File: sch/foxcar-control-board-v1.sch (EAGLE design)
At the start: 91 parts, among them Q1 PSMN1R2-30YLC, U1 HMC5883LSMD, U2 SPX29300

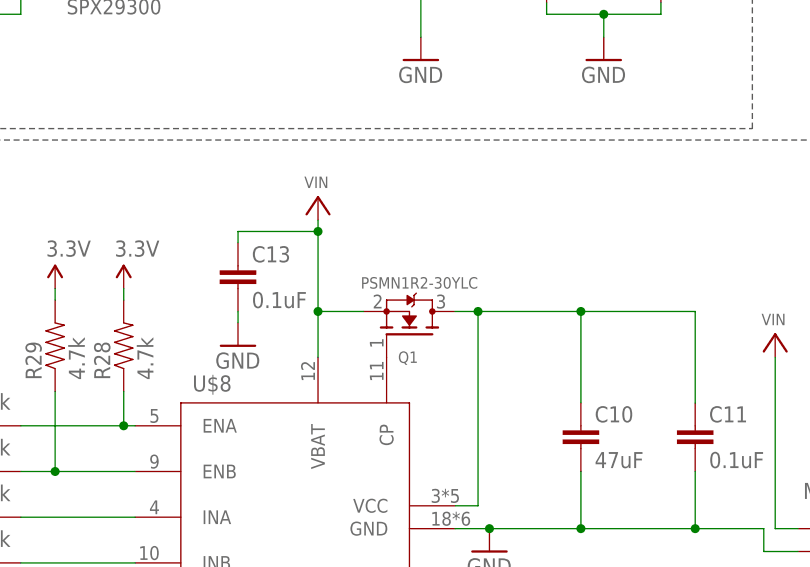
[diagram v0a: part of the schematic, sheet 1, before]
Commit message: Set up Eagle board with Sparkfun 4-layer DRU. Set up layers. Started with power section.
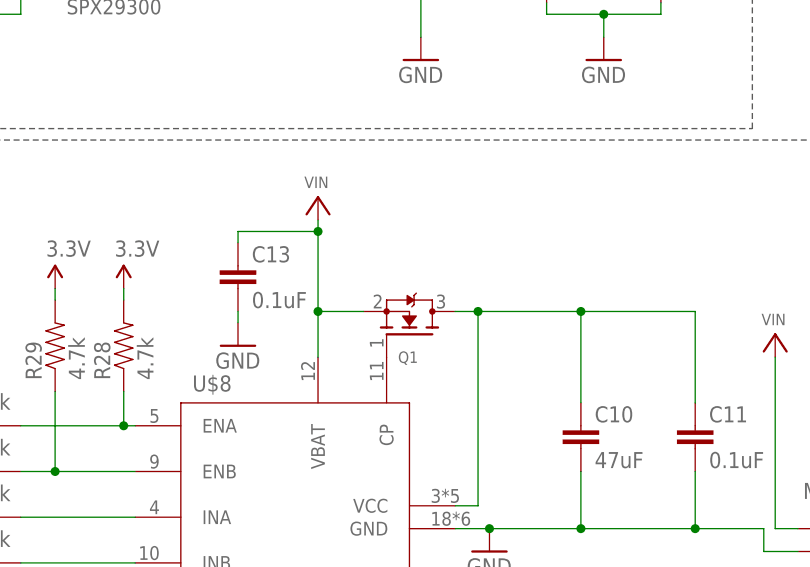
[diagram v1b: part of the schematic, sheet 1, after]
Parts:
- Q1: value PSMN1R2-30YLC -> (none)
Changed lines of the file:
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@@
 <part name="DIG_GND16" library="SparkFun-Aesthetics" deviceset="GND" device="" value="GND"/>
 <part name="DIG_GND17" library="SparkFun-Aesthetics" deviceset="GND" device="" value="GND"/>
-<part name="Q1" library="adafruit" deviceset="MOSFET-N" device="REFLOW" value="PSMN1R2-30YLC"/>
+<part name="Q1" library="adafruit" deviceset="MOSFET-N" device="REFLOW"/>
 <part name="GND12" library="SparkFun-Aesthetics" deviceset="GND" device=""/>
 <part name="JP20" library="SparkFun-Connectors" deviceset="M04" device="SCREW_LOCK" value="MOTORS"/>

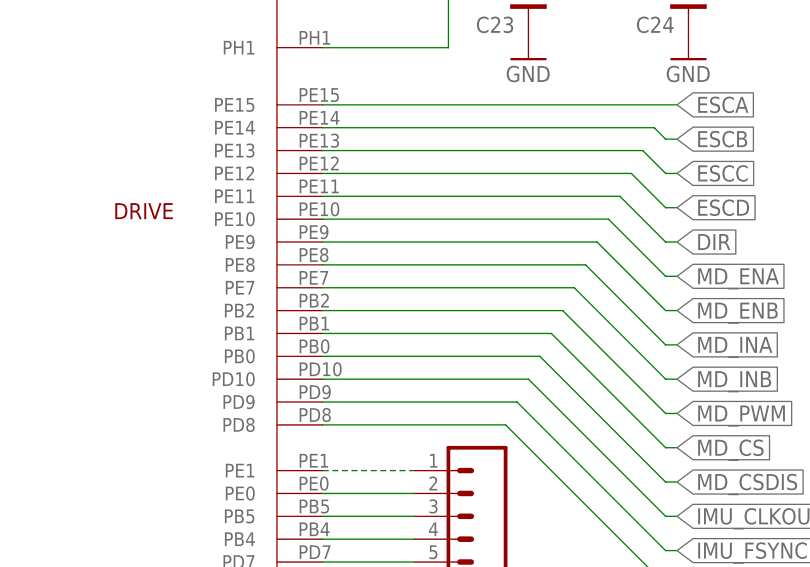
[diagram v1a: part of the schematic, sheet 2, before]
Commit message: Almost done with power layout. Minor stm32 symbol changes.
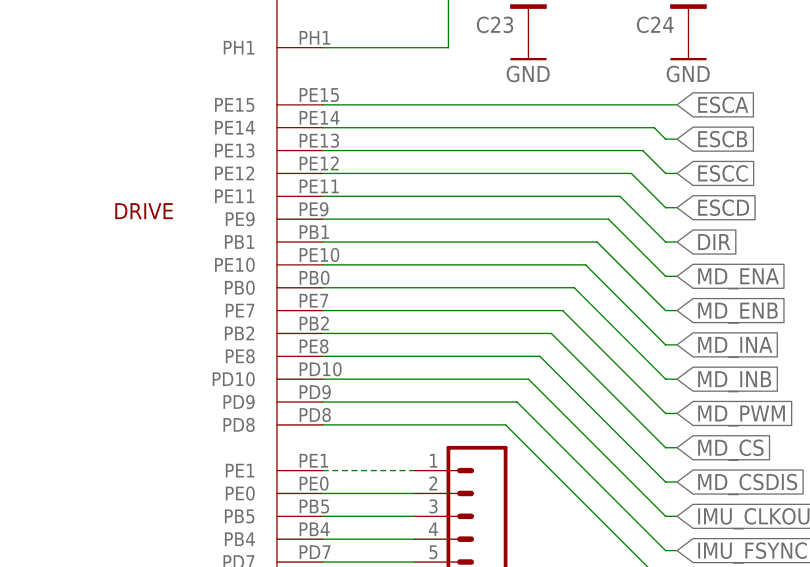
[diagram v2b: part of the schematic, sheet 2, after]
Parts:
- renumbered LED4 to LED2
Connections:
- net N$76 renamed INB
- net N$77 renamed CP
- net N$78 renamed VCC
- net N$79 renamed INA
- net N$83 renamed ENB
- net N$84 renamed ENA
- net N$85 renamed PWM
- net N$86 renamed CS
- removed net N$80: JP20.3, U$8.OUTA
- removed net N$81: JP20.4, U$8.OUTB
- new net OUTA: JP20.4, U$8.OUTA
- new net OUTB: JP20.3, U$8.OUTB
- net MD_CS: now also U$10.PB2; no longer U$10.PB1
- net MD_CSDIS: now also U$10.PE8; no longer U$10.PB0
- net MD_ENA: now also U$10.PE9; no longer U$10.PE10
- net MD_ENB: now also U$10.PB1; no longer U$10.PE9
- net MD_INA: now also U$10.PE10; no longer U$10.PE8
- net MD_INB: now also U$10.PB0; no longer U$10.PE7
- net MD_PWM: now also U$10.PE7; no longer U$10.PB2
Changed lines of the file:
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@@
 <part name="U$12" library="SparkFun-Aesthetics" deviceset="VIN" device=""/>
 <part name="LED3" library="led" deviceset="LED" device="CHIP-LED0603" value="GREEN"/>
-<part name="LED4" library="led" deviceset="LED" device="CHIP-LED0603" value="GREEN"/>
+<part name="LED2" library="led" deviceset="LED" device="CHIP-LED0603" value="GREEN"/>
 <part name="R1" library="SparkFun-Passives" deviceset="RESISTOR" device="0402-RES" value="270"/>
 <part name="R3" library="SparkFun-Passives" deviceset="RESISTOR" device="0402-RES" value="50"/>
@@
 <instance part="U$12" gate="G$1" x="-110.49" y="95.25"/>
 <instance part="LED3" gate="G$1" x="-40.64" y="91.44"/>
-<instance part="LED4" gate="G$1" x="-27.94" y="91.44"/>
+<instance part="LED2" gate="G$1" x="-27.94" y="91.44"/>
 <instance part="R1" gate="G$1" x="-40.64" y="80.01" rot="R90"/>
 <instance part="R3" gate="G$1" x="-27.94" y="80.01" rot="R90"/>
@@
 </segment>
 <segment>
-<pinref part="LED4" gate="G$1" pin="A"/>
+<pinref part="LED2" gate="G$1" pin="A"/>
 <wire x1="-27.94" y1="95.25" x2="-27.94" y2="93.98" width="0.15" layer="91"/>
 <pinref part="P+30" gate="G$1" pin="3.3V"/>
@@
 </segment>
 </net>
-<net name="N$77" class="0">
+<net name="CP" class="0">
 <segment>
 <pinref part="Q1" gate="G$1" pin="G"/>
@@
 </segment>
 </net>
-<net name="N$78" class="0">
+<net name="VCC" class="0">
 <segment>
 <pinref part="U$8" gate="G$1" pin="VCC"/>
@@
 </segment>
 </net>
-<net name="N$80" class="0">
-<segment>
-<pinref part="U$8" gate="G$1" pin="OUTA"/>
-<wire x1="-50.8" y1="8.89" x2="-16.51" y2="8.89" width="0.15" layer="91"/>
+<net name="OUTB" class="0">
+<segment>
 <wire x1="-16.51" y1="8.89" x2="-16.51" y2="11.43" width="0.15" layer="91"/>
 <pinref part="JP20" gate="G$1" pin="3"/>
 <wire x1="-16.51" y1="11.43" x2="-12.7" y2="11.43" width="0.15" layer="91"/>
-</segment>
-</net>
-<net name="N$81" class="0">
+<pinref part="U$8" gate="G$1" pin="OUTB"/>
+<wire x1="-50.8" y1="8.89" x2="-16.51" y2="8.89" width="0.15" layer="91"/>
+</segment>
+</net>
+<net name="OUTA" class="0">
 <segment>
 <pinref part="JP20" gate="G$1" pin="4"/>
 <wire x1="-12.7" y1="8.89" x2="-15.24" y2="8.89" width="0.15" layer="91"/>
 <wire x1="-15.24" y1="8.89" x2="-15.24" y2="6.35" width="0.15" layer="91"/>
-<pinref part="U$8" gate="G$1" pin="OUTB"/>
+<pinref part="U$8" gate="G$1" pin="OUTA"/>
 <wire x1="-15.24" y1="6.35" x2="-50.8" y2="6.35" width="0.15" layer="91"/>
 </segment>
 </net>
-<net name="N$86" class="0">
+<net name="CS" class="0">
 <segment>
 <pinref part="U$8" gate="G$1" pin="CS"/>
@@
 </segment>
 </net>
-<net name="N$85" class="0">
+<net name="PWM" class="0">
 <segment>
 <pinref part="U$8" gate="G$1" pin="PWM"/>
@@
 </segment>
 </net>
-<net name="N$76" class="0">
+<net name="INB" class="0">
 <segment>
 <pinref part="U$8" gate="G$1" pin="INB"/>
@@
 </segment>
 </net>
-<net name="N$79" class="0">
+<net name="INA" class="0">
 <segment>
 <pinref part="U$8" gate="G$1" pin="INA"/>
@@
 </segment>
 </net>
-<net name="N$83" class="0">
+<net name="ENB" class="0">
 <segment>
 <pinref part="U$8" gate="G$1" pin="ENB"/>
@@
 </segment>
 </net>
-<net name="N$84" class="0">
+<net name="ENA" class="0">
 <segment>
 <pinref part="U$8" gate="G$1" pin="ENA"/>
@@
 <net name="N$2" class="0">
 <segment>
-<pinref part="LED4" gate="G$1" pin="C"/>
+<pinref part="LED2" gate="G$1" pin="C"/>
 <wire x1="-27.94" y1="86.36" x2="-27.94" y2="85.09" width="0.15" layer="91"/>
 <pinref part="R3" gate="G$1" pin="2"/>
@@
 <net name="MD_ENA" class="0">
 <segment>
-<pinref part="U$10" gate="G$1" pin="PE10"/>
 <wire x1="328.93" y1="147.32" x2="327.66" y2="147.32" width="0.1524" layer="91"/>
 <wire x1="327.66" y1="147.32" x2="321.31" y2="153.67" width="0.1524" layer="91"/>
-<wire x1="321.31" y1="153.67" x2="289.56" y2="153.67" width="0.1524" layer="91"/>
 <label x="328.93" y="147.32" size="1.778" layer="95" xref="yes"/>
+<pinref part="U$10" gate="G$1" pin="PE9"/>
+<wire x1="289.56" y1="153.67" x2="321.31" y2="153.67" width="0.15" layer="91"/>
 </segment>
 </net>
 <net name="MD_ENB" class="0">
 <segment>
-<pinref part="U$10" gate="G$1" pin="PE9"/>
 <wire x1="328.93" y1="143.51" x2="327.66" y2="143.51" width="0.1524" layer="91"/>
 <wire x1="327.66" y1="143.51" x2="320.04" y2="151.13" width="0.1524" layer="91"/>
-<wire x1="320.04" y1="151.13" x2="289.56" y2="151.13" width="0.1524" layer="91"/>
 <label x="328.93" y="143.51" size="1.778" layer="95" xref="yes"/>
+<pinref part="U$10" gate="G$1" pin="PB1"/>
+<wire x1="320.04" y1="151.13" x2="289.56" y2="151.13" width="0.15" layer="91"/>
 </segment>
 </net>
 <net name="MD_INA" class="0">
 <segment>
-<pinref part="U$10" gate="G$1" pin="PE8"/>
 <wire x1="328.93" y1="139.7" x2="327.66" y2="139.7" width="0.1524" layer="91"/>
 <wire x1="327.66" y1="139.7" x2="318.77" y2="148.59" width="0.1524" layer="91"/>
-<wire x1="318.77" y1="148.59" x2="289.56" y2="148.59" width="0.1524" layer="91"/>
 <label x="328.93" y="139.7" size="1.778" layer="95" xref="yes"/>
+<pinref part="U$10" gate="G$1" pin="PE10"/>
+<wire x1="289.56" y1="148.59" x2="318.77" y2="148.59" width="0.15" layer="91"/>
 </segment>
 </net>
 <net name="MD_INB" class="0">
 <segment>
-<pinref part="U$10" gate="G$1" pin="PE7"/>
 <wire x1="328.93" y1="135.89" x2="327.66" y2="135.89" width="0.1524" layer="91"/>
 <wire x1="327.66" y1="135.89" x2="317.5" y2="146.05" width="0.1524" layer="91"/>
-<wire x1="317.5" y1="146.05" x2="289.56" y2="146.05" width="0.1524" layer="91"/>
 <label x="328.93" y="135.89" size="1.778" layer="95" xref="yes"/>
+<pinref part="U$10" gate="G$1" pin="PB0"/>
+<wire x1="317.5" y1="146.05" x2="289.56" y2="146.05" width="0.15" layer="91"/>
 </segment>
 </net>
 <net name="MD_PWM" class="0">
 <segment>
-<pinref part="U$10" gate="G$1" pin="PB2"/>
 <wire x1="328.93" y1="132.08" x2="327.66" y2="132.08" width="0.1524" layer="91"/>
 <wire x1="327.66" y1="132.08" x2="316.23" y2="143.51" width="0.1524" layer="91"/>
-<wire x1="316.23" y1="143.51" x2="289.56" y2="143.51" width="0.1524" layer="91"/>
 <label x="328.93" y="132.08" size="1.778" layer="95" xref="yes"/>
+<pinref part="U$10" gate="G$1" pin="PE7"/>
+<wire x1="289.56" y1="143.51" x2="316.23" y2="143.51" width="0.15" layer="91"/>
 </segment>
 </net>
 <net name="MD_CS" class="0">
 <segment>
-<pinref part="U$10" gate="G$1" pin="PB1"/>
 <wire x1="328.93" y1="128.27" x2="327.66" y2="128.27" width="0.1524" layer="91"/>
 <wire x1="327.66" y1="128.27" x2="314.96" y2="140.97" width="0.1524" layer="91"/>
-<wire x1="314.96" y1="140.97" x2="289.56" y2="140.97" width="0.1524" layer="91"/>
 <label x="328.93" y="128.27" size="1.778" layer="95" xref="yes"/>
+<pinref part="U$10" gate="G$1" pin="PB2"/>
+<wire x1="314.96" y1="140.97" x2="289.56" y2="140.97" width="0.15" layer="91"/>
 </segment>
 </net>
 <net name="MD_CSDIS" class="0">
 <segment>
-<pinref part="U$10" gate="G$1" pin="PB0"/>
 <wire x1="328.93" y1="124.46" x2="327.66" y2="124.46" width="0.1524" layer="91"/>
 <wire x1="327.66" y1="124.46" x2="313.69" y2="138.43" width="0.1524" layer="91"/>
-<wire x1="313.69" y1="138.43" x2="289.56" y2="138.43" width="0.1524" layer="91"/>
 <label x="328.93" y="124.46" size="1.778" layer="95" xref="yes"/>
-</segment>
-</net>
+<pinref part="U$10" gate="G$1" pin="PE8"/>
+<wire x1="289.56" y1="138.43" x2="313.69" y2="138.43" width="0.15" layer="91"/>
+</segment>
+</net>

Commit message: Making progress on layout.
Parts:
- R15: device microbuilder:RESISTOR0402 -> SparkFun-Passives:RESISTOR0402-RES
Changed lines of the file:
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@@
 <part name="DIG_GND8" library="SparkFun-Aesthetics" deviceset="GND" device="" value="GND"/>
 <part name="JTAG2" library="microbuilder" deviceset="JTAG-CORTEXM3" device="" value="MINI-JTAG"/>
-<part name="R15" library="microbuilder" deviceset="RESISTOR" device="0402" value="100"/>
+<part name="R15" library="SparkFun-Passives" deviceset="RESISTOR" device="0402-RES" value="100"/>
 <part name="DIG_GND9" library="SparkFun-Aesthetics" deviceset="GND" device="" value="GND"/>
 <part name="TP32" library="testpad" deviceset="TP" device="TP06R"/>
@@
 <wire x1="83.82" y1="33.02" x2="83.82" y2="30.48" width="0.15" layer="91"/>
 <wire x1="83.82" y1="30.48" x2="87.63" y2="30.48" width="0.15" layer="91"/>
-<wire x1="87.63" y1="30.48" x2="87.63" y2="31.75" width="0.15" layer="91"/>
 <pinref part="JTAG2" gate="G$1" pin="1"/>
-<junction x="87.63" y="30.48"/>
-</segment>
-</net>
+</segment>
+</net>

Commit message: Going to set aside that layout and try a fresh start.
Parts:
- removed C25, C26: 100nF, rcl:C-EUC0402
- removed C27: 4.7uF, microbuilder:CAP_CERAMIC0805
- removed C28: 0.22uF, microbuilder:CAP_CERAMIC0402
- removed C29: 10nF, microbuilder:CAP_CERAMIC0402
- removed C30: 0.1uF, microbuilder:CAP_CERAMIC0402
- removed R22: 1k, SparkFun-Passives:RESISTOR0402-RES
- removed R25, R27: 10k, SparkFun-Passives:RESISTOR0402-RES
- removed R28: 4.7k, SparkFun-Passives:RESISTOR0402-RES
- removed TP17, TP32, TP33: TPTP06R, testpad:TPTP06R
- added C2: 0.1uF, SparkFun-Passives:CAP0402-CAP
- added C3: 47uF, SparkFun-Passives:CAP0805
- added C4, C5: 16pF, SparkFun-Passives:CAP0402-CAP
- added C6: 10u, SparkFun-Passives:CAP0603-CAP
- added C7: 100nF, SparkFun-Passives:CAP0402-CAP
- added JP10, JP16, JP17, JP18, JP19, JP22, JP23, JP24, JP25, JP26, JP27, JP28, JP29, JP30, JP31, JP32, JP33, JP34, JP35, JP36, JP37, JP38, JP39, JP40, JP41, JP42, JP43: M01PTH_LONGPAD, SparkFun-Connectors:M01PTH_LONGPAD
- added LED4, LED5: (no value), led:LEDCHIPLED_0603
- added R14: 100, SparkFun-Passives:RESISTOR0402-RES
- added R18: 1k, SparkFun-Passives:RESISTOR0402-RES
- added R5, R7: 50, SparkFun-Passives:RESISTOR0402-RES
- added TP11: TPTP06R, testpad:TPTP06R
- C1: value 100nF -> 0.33uF; device rcl:C-EUC0402 -> SparkFun-Passives:CAP0603-CAP
- C10: value 47uF -> 100nF; device SparkFun-Passives:CAP0805 -> SparkFun-Passives:CAP0402-CAP
- C11: value 0.1uF -> 100nF
- C12: value 33nF -> 0.1uF
- C13: value 0.1uF -> 33nF
- C14: value 100nF -> 0.22uF; device rcl:C-EUC0402 -> SparkFun-Passives:CAP0402-CAP
- C15: value 0.33uF -> 0.22uF; device rcl3:C-EUC0603 -> SparkFun-Passives:CAP0402-CAP
- C16: value 10u -> 4.7uF; device rcl3:C-EUC0603 -> SparkFun-Passives:CAP0805
- C17, C22: value 100nF -> 0.1uF; device rcl:C-EUC0402 -> SparkFun-Passives:CAP0402-CAP
- C18: value 100nF -> 2.2uF; device rcl:C-EUC0402 -> SparkFun-Passives:CAP0603-CAP
- C19: device rcl:C-EUC0603 -> SparkFun-Passives:CAP0402-CAP
- C20: value 0.22uF -> 100nF; device microbuilder:CAP_CERAMIC0402 -> SparkFun-Passives:CAP0402-CAP
- C21, C9: value 2.2uF -> 100nF; device rcl:C-EUC0603 -> SparkFun-Passives:CAP0402-CAP
- C23: value 16pF -> 2.2uF; device rcl:C-EUC0402 -> SparkFun-Passives:CAP0603-CAP
- C24: value 16pF -> 10nF; device rcl:C-EUC0402 -> SparkFun-Passives:CAP0402-CAP
- C8: value 0.1uF -> 100nF; device microbuilder:CAP_CERAMIC0402 -> SparkFun-Passives:CAP0402-CAP
- JP1: value M10LOCK_LONGPADS -> M01PTH_LONGPAD; device SparkFun-Connectors:M10LOCK_LONGPADS -> SparkFun-Connectors:M01PTH_LONGPAD
- JP11: value UART2 -> ESCD; device SparkFun-Connectors:M04LOCK_LONGPADS -> SparkFun-Connectors:M03LOCK_LONGPADS
- JP12: value I2C1-B -> ESCC; device SparkFun-Connectors:M04LOCK_LONGPADS -> SparkFun-Connectors:M03LOCK_LONGPADS
- JP13: value USART3 -> ESCB; device SparkFun-Connectors:M04LOCK_LONGPADS -> SparkFun-Connectors:M03LOCK_LONGPADS
- JP14: value SPI1 -> ESCA; device SparkFun-Connectors:M06LOCK_LONGPADS -> SparkFun-Connectors:M03LOCK_LONGPADS
- JP15: value I2C1-A -> USART3
- JP2: value SERVO -> USART1; device SparkFun-Connectors:M03LOCK_LONGPADS -> SparkFun-Connectors:M04LOCK_LONGPADS
- JP20: value MOTORS -> M01PTH_LONGPAD; device SparkFun-Connectors:M04SCREW_LOCK -> SparkFun-Connectors:M01PTH_LONGPAD
- JP21: value BATT -> M01PTH_LONGPAD; device SparkFun-Connectors:M023.5MM_LOCK -> SparkFun-Connectors:M01PTH_LONGPAD
- JP3: value ESCA -> I2C1-B; device SparkFun-Connectors:M03LOCK_LONGPADS -> SparkFun-Connectors:M04LOCK_LONGPADS
- JP4: value ESCC -> BATT; device SparkFun-Connectors:M03LOCK_LONGPADS -> SparkFun-Connectors:M023.5MM_LOCK
- JP5: value ESCD -> I2C1-A; device SparkFun-Connectors:M03LOCK_LONGPADS -> SparkFun-Connectors:M04LOCK_LONGPADS
- JP6: value ESCB -> UART2; device SparkFun-Connectors:M03LOCK_LONGPADS -> SparkFun-Connectors:M04LOCK_LONGPADS
- JP7: value M10LOCK_LONGPADS -> MOTORS; device SparkFun-Connectors:M10LOCK_LONGPADS -> SparkFun-Connectors:M04SCREW_LOCK
- JP8: value USART1 -> SPI1; device SparkFun-Connectors:M04LOCK_LONGPADS -> SparkFun-Connectors:M06LOCK_LONGPADS
- JP9: value M10LOCK_LONGPADS -> SERVO; device SparkFun-Connectors:M10LOCK_LONGPADS -> SparkFun-Connectors:M03LOCK_LONGPADS
- LED1: value RGB -> GREEN; device LED_RGB_PLCC6:LED_RGB_PLCC-6 -> led:LEDCHIPLED_0603
- LED2: value GREEN -> (none); device led:LEDCHIP-LED0603 -> led:LEDCHIPLED_0603
- LED3: device led:LEDCHIP-LED0603 -> led:LEDCHIPLED_0603
- R15: value 100 -> 10k
- R16: value 1.5k -> 10k
- R19: value 10k -> 1k
- R20: value 1k -> 4.7k
- R4: value 1.5k -> 50
- R6, R9: value 10k -> 1.5k
- U1: value HMC5883LSMD -> SPX29300; device SparkFun-Sensors:HMC5883LSMD -> microbuilder:VREG_TO263-5
- U2: value SPX29300 -> HMC5883LSMD; device microbuilder:VREG_TO263-5 -> SparkFun-Sensors:HMC5883LSMD
- U3: value STM32F4V_100PIN_FOXCAR -> STM32F4V
- renumbered CTS406 to CTS1, JTAG2 to JTAG1, R21 to R13, R23 to R12, R24 to R17, R26 to R11, R29 to R10, TP15 to TP10, TP16 to TP12, TP18 to TP3, TP19 to TP9, TP20 to TP8, TP21 to TP13, TP34 to TP4, TP39 to TP1, TP40 to TP5, TP41 to TP7, TP42 to TP6, TP43 to TP2, U$10 to U3, U$13 to J2, U$3 to U6, U$8 to U4, USB_MICRO1 to J1, XB2 to J3
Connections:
- net 3.3V: now also C10.2, C11.2, C14.1, C20.2, C22.1, C23.2, C6.1, C7.2, C8.2, JP2.4, JP3.4, JP5.4, JP6.4, JP8.6, JP9.2, LED3.A, R14.2, R20.2, R3.1, R4.1, R5.1, R6.2, R8.2, R9.2, U1.VOUT, U2.S1, U2.VDD, U2.VDDIO; no longer C1.2, C14.2, C16.1, C17.2, C22.2, C25.2, C26.2, C28.P$1, C8.P$1, JP11.4, JP12.4, JP13.4, JP14.6, JP2.2, JP8.4, LED2.A, R15.2, R16.2, R19.2, R28.2, R4.2, R6.1, R8.1, R9.1, TP33.TP, U1.S1, U1.VDD, U1.VDDIO, U2.VOUT
- net CS: now also R15.2; no longer R25.2
- net DIR: now also JP9.1; no longer JP2.1
- net ENA: now also R18.2, R20.1; no longer R20.2, R28.1
- net ESCA: now also JP14.1, TP11.TP; no longer JP3.1, TP14.TP
- net ESCB: now also JP13.1; no longer JP6.1
- net ESCC: now also JP12.1; no longer JP4.1
- net ESCD: now also JP11.1; no longer JP5.1
- net FS_DP: now also R9.1; no longer R16.1
- net GND: now also C1.2, C10.1, C11.1, C14.2, C17.2, C2.2, C20.1, C22.2, C24.2, C3.2, C4.1, C5.1, C6.2, C7.1, C8.1, JP2.1, JP3.1, JP4.1, JP5.1, JP6.1, JP7.2, JP9.3, R16.1, R7.1, TP14.TP, U1.GND0, U1.GND1, U2.GND@1, U2.GND@2; no longer C1.1, C10.2, C11.2, C14.1, C15.2, C17.1, C22.1, C24.1, C25.1, C26.1, C27.P$2, C28.P$2, C29.P$2, C30.P$2, C8.P$2, JP11.1, JP12.1, JP13.1, JP14.1, JP2.3, JP20.2, JP21.1, R27.1, R3.1, TP17.TP, TP32.TP, U1.GND@1, U1.GND@2, U2.GND0, U2.GND1
- net INA: now also R19.2; no longer R22.2
- net LED_B: now also LED5.A; no longer LED1R.K
- net LED_G: now also LED4.A; no longer LED1G.K
- net LED_R: now also LED2.A; no longer LED1B.K
- net MD_CS: now also C13.1, R15.1; no longer C12.1, R25.1
- net MD_ENA: now also R18.1; no longer R20.1
- net MD_INA: now also R19.1; no longer R22.1
- net MD_PWM: now also R16.2; no longer R27.2
- net N$1: now also JP25.1; no longer JP7.2
- net N$10: now also JP37.1; no longer JP9.4
- net N$11: now also C15.1, U2.SETP; no longer C20.P$1, U1.SETP
- net N$12: now also C16.1, U2.C1; no longer C27.P$1, U1.C1
- net N$13: now also C17.1; no longer C30.P$1
- net N$14: now also JP36.1; no longer JP9.3
- net N$16: now also JP35.1; no longer JP9.2
- net N$17: now also JP34.1; no longer JP9.1
- net N$18: now also C24.1; no longer C29.P$1
- net N$2: now also LED3.C, R7.2; no longer LED2.C, R3.2
- net N$20: now also R14.1; no longer R15.1
- net N$3: now also LED1.C; no longer LED3.C
- net N$4: now also C15.2, U2.SETC; no longer C20.P$2, U1.SETC
- net N$41: now also JP43.1; no longer JP9.10
- net N$42: now also JP42.1; no longer JP9.9
- net N$43: now also JP41.1; no longer JP9.8
- net N$44: now also JP40.1; no longer JP9.7
- net N$45: now also JP39.1; no longer JP9.6
- net N$5: now also LED2.C, R4.2; no longer LED1B.A, R9.2
- net N$55: now also JP26.1; no longer JP7.3
- net N$56: now also JP27.1; no longer JP7.4
- net N$57: now also JP28.1; no longer JP7.5
- net N$58: now also JP29.1; no longer JP7.6
- net N$59: now also JP30.1; no longer JP7.7
- net N$6: now also LED4.C, R5.2; no longer LED1G.A, R6.2
- net N$60: now also JP31.1; no longer JP7.8
- net N$61: now also JP32.1; no longer JP7.9
- net N$66: now also JP10.1; no longer JP1.2
- net N$67: now also JP16.1; no longer JP1.3
- net N$68: now also JP17.1; no longer JP1.4
- net N$69: now also JP18.1; no longer JP1.5
- net N$7: now also LED5.C, R3.2; no longer LED1R.A, R8.2
- net N$70: now also JP19.1; no longer JP1.6
- net N$71: now also JP20.1; no longer JP1.7
- net N$72: now also JP21.1; no longer JP1.8
- net N$73: now also JP22.1; no longer JP1.9
- net N$74: now also JP23.1; no longer JP1.10
- net N$75: now also JP24.1; no longer JP7.1
- net N$8: now also JP33.1; no longer JP7.10
- net N$9: now also JP38.1; no longer JP9.5
- net NRST: now also R8.1; no longer R19.1
- net OSC_IN1: now also C4.2; no longer C24.2
- net OSC_OUT1: now also C5.2; no longer C23.2
- net OUTA: now also JP7.4; no longer JP20.4
- net OUTB: now also JP7.3; no longer JP20.3
- net RX1: now also JP2.2, U3.PA1; no longer JP8.2, U3.PB7
- net RX2: now also JP6.2; no longer JP11.2
- net RX3: now also JP15.2; no longer JP13.2
- net RX_DOUT1: now also U3.PB7; no longer U3.PA1
- net SCL1: now also JP3.2, JP5.2, R6.1, U2.SCL; no longer JP12.2, JP15.2, R4.1, U1.SCL
- net SDA1: now also JP3.3, JP5.3, U2.SDA; no longer JP12.3, JP15.3, U1.SDA
- net SPI1_MISO: now also JP8.3; no longer JP14.3
- net SPI1_MOSI: now also JP8.2; no longer JP14.2
- net SPI1_NSS: now also JP8.5; no longer JP14.5
- net SPI1_SCK: now also JP8.4; no longer JP14.4
- net TX1: now also JP2.3, U3.PA0; no longer JP8.3, U3.PB6
- net TX2: now also JP6.3; no longer JP11.3
- net TX3: now also JP15.3; no longer JP13.3
- net TX_DIN1: now also U3.PB6; no longer U3.PA0
- net VCC: now also C2.1, C3.1; no longer C10.1, C11.1
- net VIN: now also C1.1, C12.1, JP4.2, JP7.1, LED1.A, U1.VIN; no longer C13.1, C15.1, JP20.1, JP21.2, LED3.A, U2.VIN
